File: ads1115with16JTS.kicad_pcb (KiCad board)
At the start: 2 copper layers, 45.7 x 68.6 mm, 50 parts, among them J1 Conn_01x02_Pin, J10 Conn_01x02_Pin, J11 Conn_01x02_Pin, J12 Conn_01x02_Pin, J13 Conn_01x02_Pin, J14 Conn_01x02_Pin, J15 Conn_01x02_Pin, J16 Conn_01x02_Pin, J17 Conn_01x04_Pin, J18 PinSocket_1x20_P2.54mm_Vertic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, J19 PinSocket_1x20_P2.54mm_Vertic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, J2 Conn_01x02_Pin, J20 Screw_Terminal_01x02, J3 Conn_01x02_Pin, J4 Conn_01x02_Pin, J5 Conn_01x02_Pin, J6 Conn_01x02_Pin, J7 Conn_01x02_Pin, J8 Conn_01x02_Pin, J9 Conn_01x02_Pin, U1 ADS1115IDGS, U2 ADS1115IDGS, U3 ADS1115IDGS, U4 ADS1115IDGS

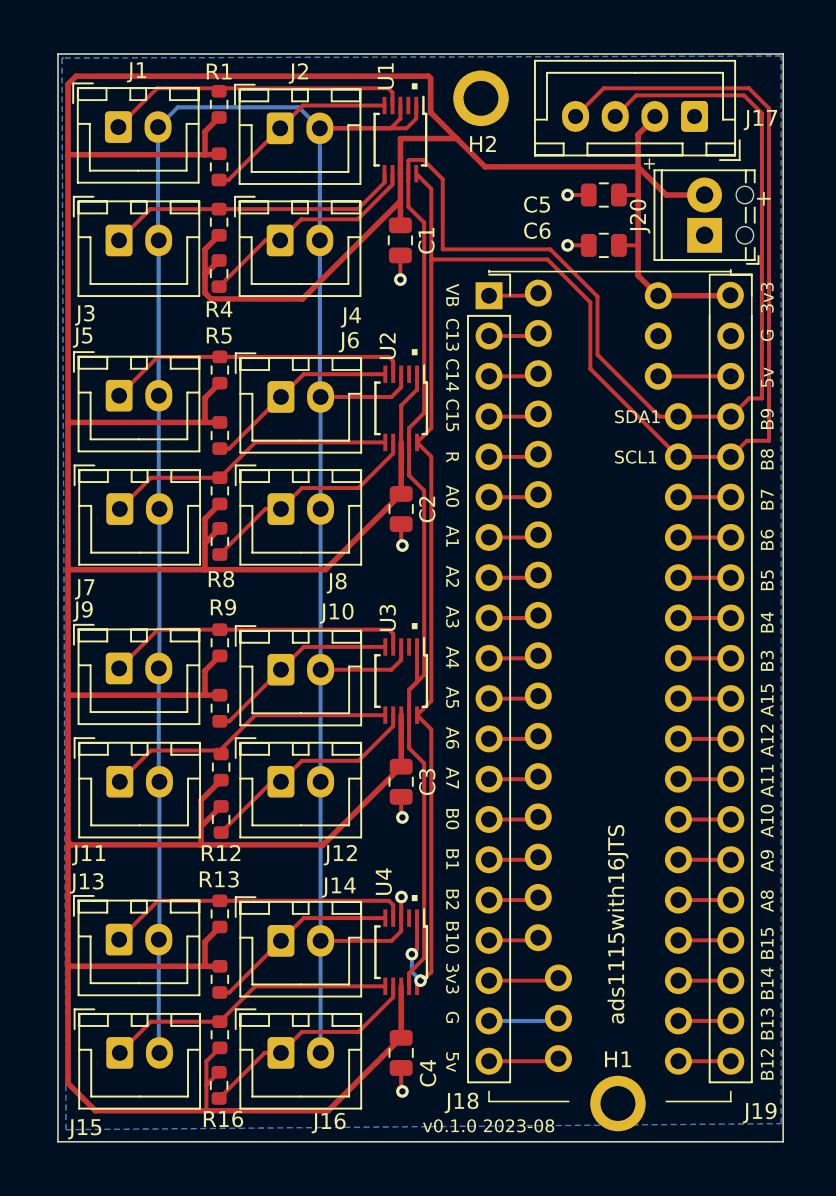
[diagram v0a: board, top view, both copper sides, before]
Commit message: moved connectors J17 and J20 and mounting hole H2 so power wire connection is in a better place.
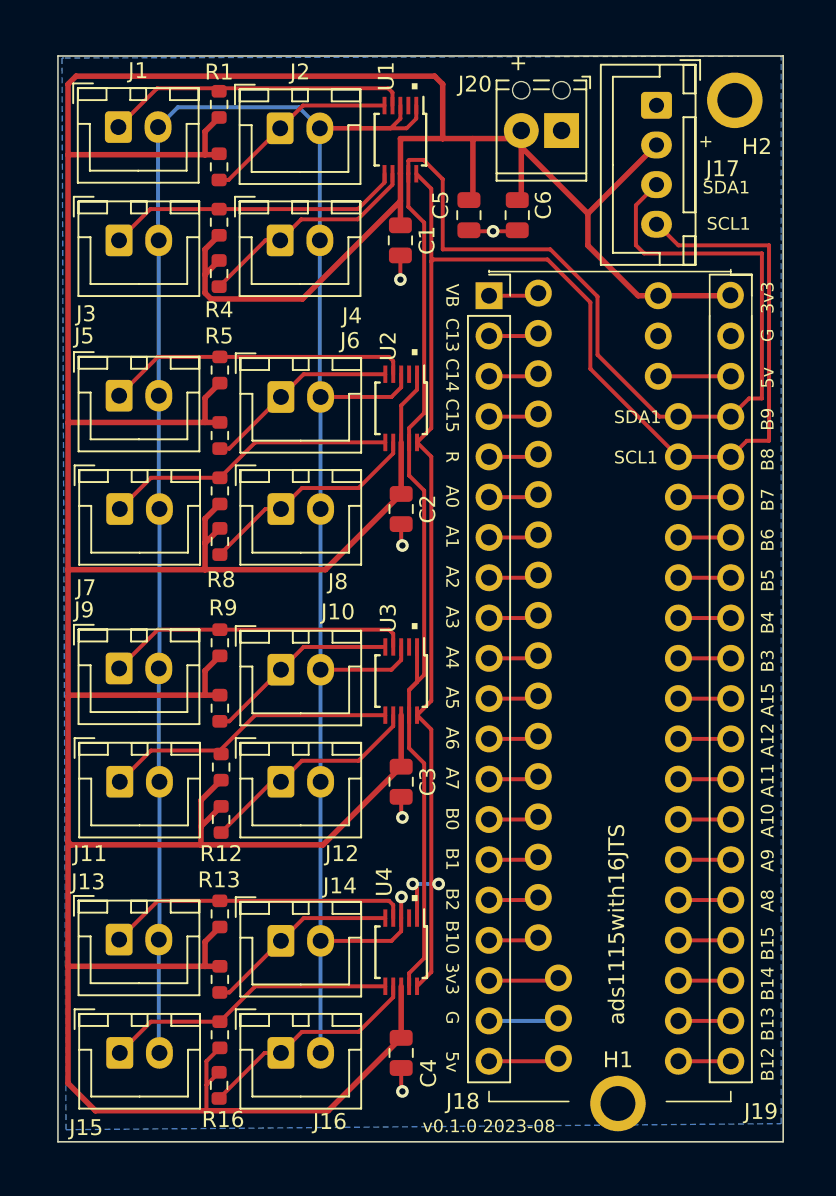
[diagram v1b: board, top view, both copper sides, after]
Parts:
- moved H2 16.0 mm to (93.5, 28.3)
- moved J20 11.2 mm to (82.5, 30.2), turned to 180 degrees
- moved C5 8.60 mm to (76.7, 35.6), turned to -90 degrees
- moved C6 5.78 mm to (79.8, 35.6), turned to -90 degrees
- moved J17 2.50 mm to (88.5, 28.6), turned to -90 degrees
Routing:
- net /SCL1: track 121.5 -> 106.7 mm
- net /SDA1: track 118.9 -> 112.3 mm
- net +3V3: track 307.7 -> 309.5 mm
- net GND: track 174.0 -> 174.5 mm, vias 7 -> 6
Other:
- board size 45.7 x 68.6 mm -> 45.7 x 68.5 mm

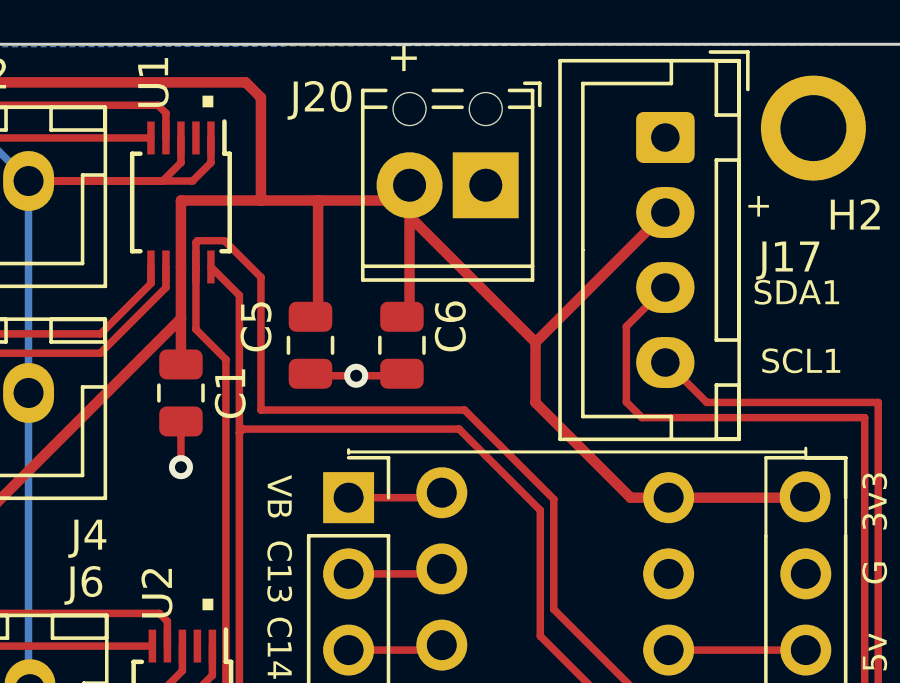
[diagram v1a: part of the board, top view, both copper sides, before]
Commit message: added 2 more noise caps on power line. Ongoing attempt to update PCB from schematic and keep footprint links to ProjectLib.
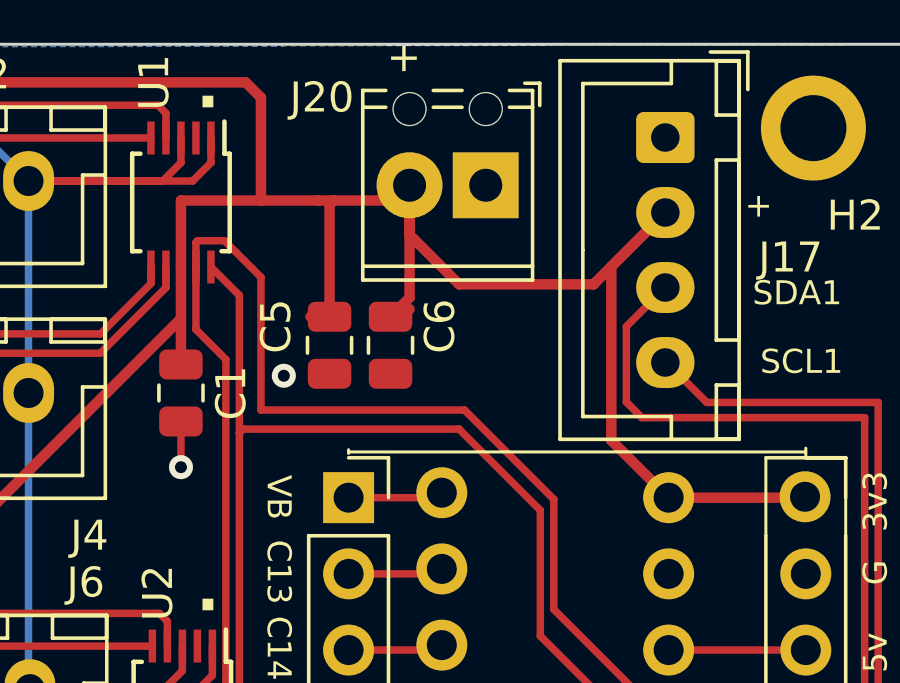
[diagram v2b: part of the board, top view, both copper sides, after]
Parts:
- moved C5 0.64 mm to (77.3, 35.6)
- moved C6 0.38 mm to (79.4, 35.6)
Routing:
- net GND: track 174.5 -> 171.5 mm
- net +3V3: track 309.5 -> 312.4 mm
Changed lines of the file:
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@@
   )
   (footprint "ProjectLib:C_0805_2012Metric" (layer "F.Cu")
-    (at 79.756 35.56 -90)
+    (at 79.375 35.56 -90)
     (descr "Capacitor SMD 0805 (2012 Metric), square (rectangular) end terminal, IPC_7351 nominal, (Body size source: IPC-SM-782 page 76, https://www.pcb-3d.com/wordpress/wp-content/uploads/ipc-sm-782a_amendment_1_and_2.pdf, https://docs.google.com/spreadsheets/d/1BsfQQcO9C6DZCsRaXUlFlo91Tg2WpOkGARC1WS5S8t0/edit?usp=sharing), generated with kicad-footprint-generator")
     (tags "capacitor")
@@
   )
   (footprint "ProjectLib:C_0805_2012Metric" (layer "F.Cu")
-    (at 76.708 35.56 -90)
+    (at 77.343 35.56 -90)
     (descr "Capacitor SMD 0805 (2012 Metric), square (rectangular) end terminal, IPC_7351 nominal, (Body size source: IPC-SM-782 page 76, https://www.pcb-3d.com/wordpress/wp-content/uploads/ipc-sm-782a_amendment_1_and_2.pdf, https://docs.google.com/spreadsheets/d/1BsfQQcO9C6DZCsRaXUlFlo91Tg2WpOkGARC1WS5S8t0/edit?usp=sharing), generated with kicad-footprint-generator")
     (tags "capacitor")
@@
   (segment (start 61.087 72.835) (end 59.817 74.105) (width 0.35) (layer "F.Cu") (net 1))
   (segment (start 72.39 32.95) (end 72.39 30.734) (width 0.35) (layer "F.Cu") (net 1))
+  (segment (start 81.661 33.528) (end 86.143 33.528) (width 0.35) (layer "F.Cu") (net 1))
   (segment (start 60.96 36.83) (end 60.071 37.719) (width 0.35) (layer "F.Cu") (net 1))
   (segment (start 60.071 65.8225) (end 51.5255 65.8225) (width 0.35) (layer "F.Cu") (net 1))
@@
   (segment (start 61.0075 53.7675) (end 60.071 54.704) (width 0.35) (layer "F.Cu") (net 1))
   (segment (start 60.071 40.467173) (end 60.446827 40.843) (width 0.35) (layer "F.Cu") (net 1))
+  (segment (start 77.343 34.61) (end 77.343 30.861) (width 0.35) (layer "F.Cu") (net 1))
   (segment (start 51.943 26.797) (end 74.549 26.797) (width 0.35) (layer "F.Cu") (net 1))
   (segment (start 60.071 64.279) (end 60.071 65.8225) (width 0.35) (layer "F.Cu") (net 1))
@@
   (segment (start 88.646 40.64) (end 93.163 40.64) (width 0.35) (layer "F.Cu") (net 1))
   (segment (start 67.51 75.26) (end 59.817 75.26) (width 0.35) (layer "F.Cu") (net 1))
-  (segment (start 84.209 35.462) (end 80.01 31.263) (width 0.35) (layer "F.Cu") (net 1))
   (segment (start 61.0075 82.9175) (end 60.071 82.9175) (width 0.35) (layer "F.Cu") (net 1))
   (segment (start 72.4375 84.1775) (end 72.4375 87.4275) (width 0.35) (layer "F.Cu") (net 1))
   (segment (start 60.071 47.084) (end 60.071 48.6275) (width 0.35) (layer "F.Cu") (net 1))
   (segment (start 72.39 34.671) (end 72.39 36.2) (width 0.35) (layer "F.Cu") (net 1))
+  (segment (start 86.143 33.528) (end 88.536 31.135) (width 0.35) (layer "F.Cu") (net 1))
   (segment (start 79.756 34.61) (end 80.01 34.356) (width 0.35) (layer "F.Cu") (net 1))
   (segment (start 60.071 54.704) (end 60.071 56.2455) (width 0.35) (layer "F.Cu") (net 1))
@@
   (segment (start 61.0075 46.1475) (end 60.071 47.084) (width 0.35) (layer "F.Cu") (net 1))
   (segment (start 51.435 75.057) (end 51.435 82.931) (width 0.35) (layer "F.Cu") (net 1))
+  (segment (start 76.962 30.734) (end 77.47 30.734) (width 0.35) (layer "F.Cu") (net 1))
   (segment (start 67.663 57.912) (end 60.071 57.912) (width 0.35) (layer "F.Cu") (net 1))
   (segment (start 51.435 82.931) (end 51.435 90.297) (width 0.35) (layer "F.Cu") (net 1))
@@
   (segment (start 75.057 27.305) (end 75.057 30.734) (width 0.35) (layer "F.Cu") (net 1))
   (segment (start 72.4375 49.8875) (end 72.4375 47.5625) (width 0.25) (layer "F.Cu") (net 1))
-  (segment (start 80.01 31.263) (end 80.01 30.226) (width 0.35) (layer "F.Cu") (net 1))
   (segment (start 60.071 37.719) (end 60.071 39.307) (width 0.35) (layer "F.Cu") (net 1))
   (segment (start 60.071 39.307) (end 60.071 40.467173) (width 0.35) (layer "F.Cu") (net 1))
@@
   (segment (start 60.9 31.75) (end 60.071 31.75) (width 0.35) (layer "F.Cu") (net 1))
   (segment (start 74.549 26.797) (end 75.057 27.305) (width 0.35) (layer "F.Cu") (net 1))
-  (segment (start 76.962 30.734) (end 79.502 30.734) (width 0.35) (layer "F.Cu") (net 1))
   (segment (start 60.071 39.307) (end 60.96 38.418) (width 0.35) (layer "F.Cu") (net 1))
   (segment (start 51.638 75.26) (end 59.817 75.26) (width 0.35) (layer "F.Cu") (net 1))
   (segment (start 51.4485 82.9175) (end 51.435 82.931) (width 0.35) (layer "F.Cu") (net 1))
   (segment (start 72.4375 49.8875) (end 72.4375 53.1375) (width 0.35) (layer "F.Cu") (net 1))
-  (segment (start 87.376 40.64) (end 88.646 40.64) (width 0.35) (layer "F.Cu") (net 1))
+  (segment (start 88.646 40.64) (end 86.736 38.73) (width 0.35) (layer "F.Cu") (net 1))
   (segment (start 60.16 88.905) (end 60.16 90.399) (width 0.25) (layer "F.Cu") (net 1))
   (segment (start 72.39 30.734) (end 75.057 30.734) (width 0.35) (layer "F.Cu") (net 1))
   (segment (start 60.16 91.986) (end 60.198 92.024) (width 0.25) (layer "F.Cu") (net 1))
+  (segment (start 80.01 30.226) (end 80.01 31.877) (width 0.35) (layer "F.Cu") (net 1))
+  (segment (start 80.01 33.975) (end 80.01 30.226) (width 0.35) (layer "F.Cu") (net 1))
   (segment (start 60.96 89.599) (end 60.16 90.399) (width 0.25) (layer "F.Cu") (net 1))
   (segment (start 60.071 82.9175) (end 51.4485 82.9175) (width 0.35) (layer "F.Cu") (net 1))
   (segment (start 51.435 75.057) (end 51.638 75.26) (width 0.35) (layer "F.Cu") (net 1))
+  (segment (start 80.01 31.877) (end 81.661 33.528) (width 0.35) (layer "F.Cu") (net 1))
   (segment (start 72.39 32.95) (end 72.39 34.671) (width 0.35) (layer "F.Cu") (net 1))
   (segment (start 51.4485 48.6275) (end 51.435 48.641) (width 0.35) (layer "F.Cu") (net 1))
   (segment (start 61.087 71.183) (end 59.817 72.453) (width 0.35) (layer "F.Cu") (net 1))
-  (segment (start 84.209 37.473) (end 87.376 40.64) (width 0.35) (layer "F.Cu") (net 1))
+  (segment (start 86.736 38.73) (end 86.736 32.935) (width 0.35) (layer "F.Cu") (net 1))
+  (segment (start 79.375 34.61) (end 80.01 33.975) (width 0.35) (layer "F.Cu") (net 1))
   (segment (start 75.057 30.734) (end 76.962 30.734) (width 0.35) (layer "F.Cu") (net 1))
-  (segment (start 88.536 31.135) (end 84.209 35.462) (width 0.35) (layer "F.Cu") (net 1))
-  (segment (start 84.209 35.462) (end 84.209 37.473) (width 0.35) (layer "F.Cu") (net 1))
   (segment (start 61.0075 88.0575) (end 60.16 88.905) (width 0.25) (layer "F.Cu") (net 1))
+  (segment (start 86.736 32.935) (end 88.536 31.135) (width 0.35) (layer "F.Cu") (net 1))
   (segment (start 60.96 31.69) (end 60.9 31.75) (width 0.35) (layer "F.Cu") (net 1))
   (segment (start 60.071 81.374) (end 60.071 82.9175) (width 0.35) (layer "F.Cu") (net 1))
@@
   (segment (start 61.0075 48.6275) (end 60.071 48.6275) (width 0.35) (layer "F.Cu") (net 1))
   (segment (start 72.4375 47.5625) (end 73.4375 46.5625) (width 0.25) (layer "F.Cu") (net 1))
-  (segment (start 80.01 34.356) (end 80.01 30.226) (width 0.35) (layer "F.Cu") (net 1))
   (segment (start 60.071 56.2455) (end 60.071 57.912) (width 0.35) (layer "F.Cu") (net 1))
+  (segment (start 77.47 30.734) (end 79.502 30.734) (width 0.35) (layer "F.Cu") (net 1))
   (segment (start 72.4375 53.1375) (end 67.663 57.912) (width 0.35) (layer "F.Cu") (net 1))
-  (segment (start 76.962 34.356) (end 76.962 30.734) (width 0.35) (layer "F.Cu") (net 1))
+  (segment (start 77.343 30.861) (end 77.47 30.734) (width 0.35) (layer "F.Cu") (net 1))
   (segment (start 59.817 74.105) (end 59.817 75.26) (width 0.35) (layer "F.Cu") (net 1))
   (segment (start 66.218 40.843) (end 72.39 34.671) (width 0.35) (layer "F.Cu") (net 1))
@@
   (segment (start 51.435 31.75) (end 51.435 48.641) (width 0.35) (layer "F.Cu") (net 1))
   (segment (start 51.435 27.305) (end 51.943 26.797) (width 0.35) (layer "F.Cu") (net 1))
-  (segment (start 78.232 36.576) (end 79.69 36.576) (width 0.25) (layer "F.Cu") (net 2))
   (segment (start 72.78 30.085) (end 67.31 30.085) (width 0.25) (layer "F.Cu") (net 2))
   (segment (start 72.4375 89.3275) (end 72.4375 90.7255) (width 0.25) (layer "F.Cu") (net 2))
@@
   (segment (start 72.4375 80.7025) (end 72.4375 79.8775) (width 0.25) (layer "F.Cu") (net 2))
   (segment (start 67.31 30.085) (end 71.78 30.085) (width 0.25) (layer "F.Cu") (net 2))
-  (segment (start 78.232 36.576) (end 76.774 36.576) (width 0.25) (layer "F.Cu") (net 2))
   (segment (start 73.39 29.475) (end 72.78 30.085) (width 0.25) (layer "F.Cu") (net 2))
   (segment (start 72.4375 46.4125) (end 72.4375 45.5875) (width 0.25) (layer "F.Cu") (net 2))
   (segment (start 71.8275 47.0225) (end 72.4375 46.4125) (width 0.25) (layer "F.Cu") (net 2))
-  (segment (start 76.774 36.576) (end 76.708 36.51) (width 0.25) (layer "F.Cu") (net 2))
   (segment (start 72.4375 78.567431) (end 72.45721 78.547721) (width 0.25) (layer "F.Cu") (net 2))
   (segment (start 73.39 28.65) (end 73.39 29.475) (width 0.25) (layer "F.Cu") (net 2))
@@
   (via (at 72.39 39.624) (size 0.8) (drill 0.4) (layers "F.Cu" "B.Cu") (net 2))
   (via (at 72.517 73.533) (size 0.8) (drill 0.4) (layers "F.Cu" "B.Cu") (net 2))
-  (via (at 78.232 36.576) (size 0.8) (drill 0.4) (layers "F.Cu" "B.Cu") (free) (net 2))
   (via (at 72.517 90.805) (size 0.8) (drill 0.4) (layers "F.Cu" "B.Cu") (net 2))
+  (via (at 75.819 36.576) (size 0.8) (drill 0.4) (layers "F.Cu" "B.Cu") (free) (net 2))
   (via (at 72.517 56.388) (size 0.8) (drill 0.4) (layers "F.Cu" "B.Cu") (net 2))
   (segment (start 67.3575 64.2175) (end 67.3575 71.2825) (width 0.25) (layer "B.Cu") (net 2))

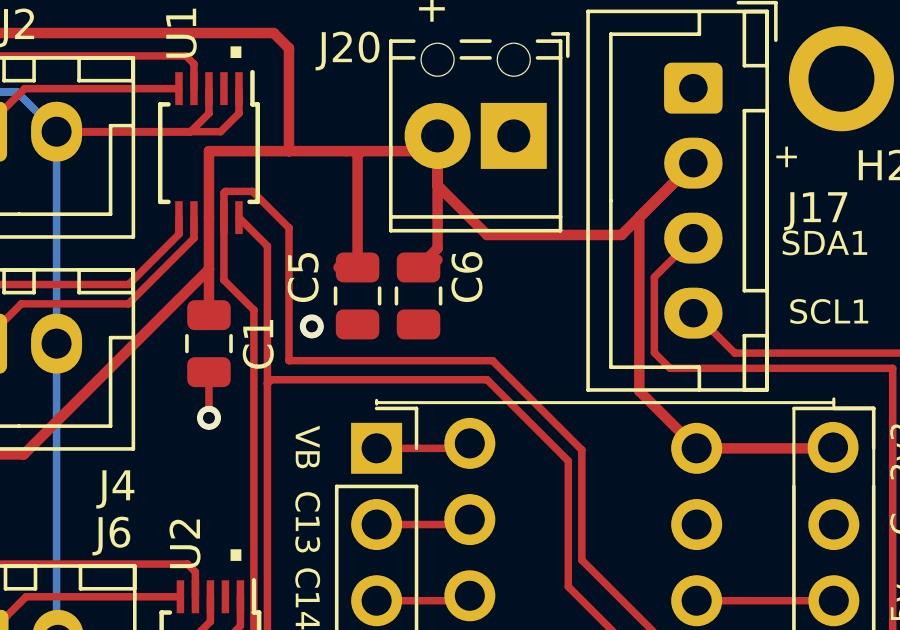
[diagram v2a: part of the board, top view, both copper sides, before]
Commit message: added 2 more power noise caps and changed to 10muF.
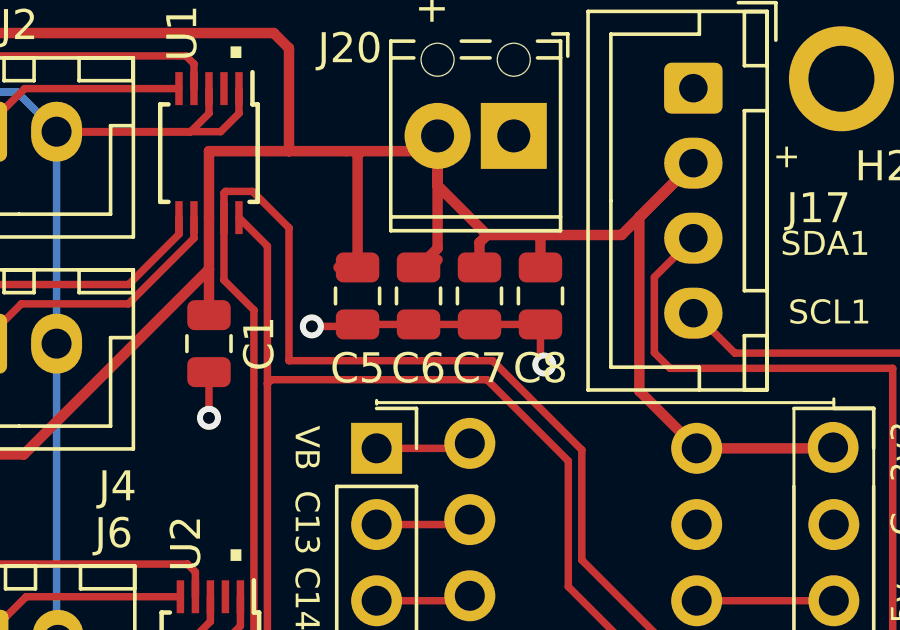
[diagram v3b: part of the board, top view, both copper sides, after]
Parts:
- added C7: 10µF5, ProjectLib:C_0805_2012Metric, F.Cu at (81.4, 35.6)
- added C8: 10µF6, ProjectLib:C_0805_2012Metric, F.Cu at (83.4, 35.6)
- C5: value 22µF5 -> 10µF5
- C6: value 22µF6 -> 10µF6
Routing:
- net GND: track 171.5 -> 180.5 mm, vias 6 -> 7
- net +3V3: track 312.4 -> 314.6 mm
